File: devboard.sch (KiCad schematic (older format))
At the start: 100 parts, among them J1 Conn_01x04, J2 Conn_02x05_Odd_Even, J3 USB_B_Micro, J4 Conn_01x04, J5 Conn_02x10_Counter_Clockwise, J6 Conn_02x04_Counter_Clockwise, Q1 Q_NPN_BEC, Q2 Q_NPN_BEC, SW1 SW_SPST, U1 ATmega128L-8AU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

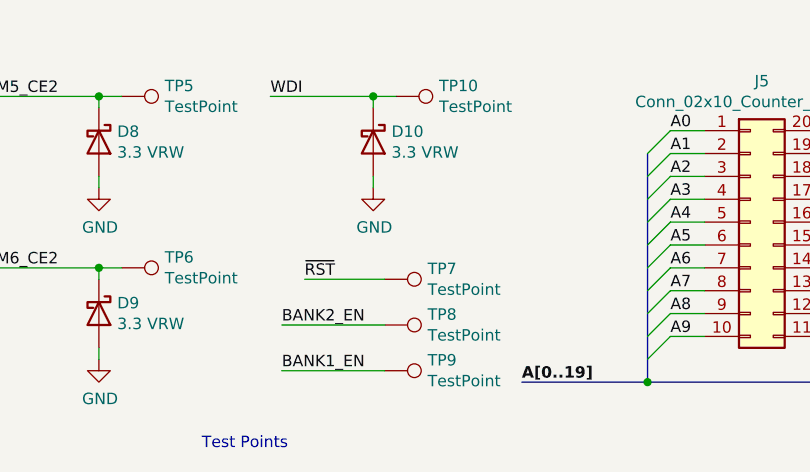
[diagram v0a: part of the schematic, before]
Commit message: Add 5V testpoint
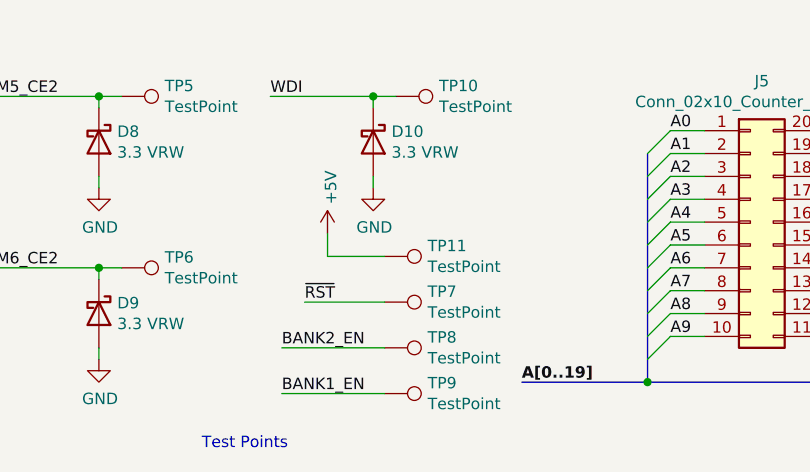
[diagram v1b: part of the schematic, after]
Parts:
- added TP11: TestPoint, Connector_PinHeader_2.54mm:PinHeader_1x01_P2.54mm_Vertical, symbol Connector:TestPoint
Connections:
- net +5V: now also TP11.1
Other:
- moved on the sheet: TP7, TP8, TP9
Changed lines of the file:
@@
 L Connector:TestPoint TP7
 U 1 1 6AC9D37E
-P 8100 10300
-F 0 "TP7" V 8054 10488 50  0000 L CNN
-F 1 "TestPoint" V 8145 10488 50  0000 L CNN
-F 2 "Connector_PinHeader_2.54mm:PinHeader_1x01_P2.54mm_Vertical" H 8300 10300 50  0001 C CNN
-F 3 "~" H 8300 10300 50  0001 C CNN
-	1    8100 10300
-	0    1    1    0
-$EndComp
-Wire Wire Line
-	7750 10300 8100 10300
-Text Label 7750 10300 0    50   ~ 0
+P 8100 10400
+F 0 "TP7" V 8054 10588 50  0000 L CNN
+F 1 "TestPoint" V 8145 10588 50  0000 L CNN
+F 2 "Connector_PinHeader_2.54mm:PinHeader_1x01_P2.54mm_Vertical" H 8300 10400 50  0001 C CNN
+F 3 "~" H 8300 10400 50  0001 C CNN
+	1    8100 10400
+	0    1    1    0
+$EndComp
+Wire Wire Line
+	7750 10400 8100 10400
+Text Label 7750 10400 0    50   ~ 0
 ~RST
 $Comp
 L Connector:TestPoint TP8
 U 1 1 6A948047
-P 8100 10500
-F 0 "TP8" V 8054 10688 50  0000 L CNN
-F 1 "TestPoint" V 8145 10688 50  0000 L CNN
-F 2 "Connector_PinHeader_2.54mm:PinHeader_1x01_P2.54mm_Vertical" H 8300 10500 50  0001 C CNN
-F 3 "~" H 8300 10500 50  0001 C CNN
-	1    8100 10500
+P 8100 10600
+F 0 "TP8" V 8054 10788 50  0000 L CNN
+F 1 "TestPoint" V 8145 10788 50  0000 L CNN
+F 2 "Connector_PinHeader_2.54mm:PinHeader_1x01_P2.54mm_Vertical" H 8300 10600 50  0001 C CNN
+F 3 "~" H 8300 10600 50  0001 C CNN
+	1    8100 10600
 	0    1    1    0
 $EndComp
@@
 L Connector:TestPoint TP9
 U 1 1 6A948041
-P 8100 10700
-F 0 "TP9" V 8054 10888 50  0000 L CNN
-F 1 "TestPoint" V 8145 10888 50  0000 L CNN
-F 2 "Connector_PinHeader_2.54mm:PinHeader_1x01_P2.54mm_Vertical" H 8300 10700 50  0001 C CNN
-F 3 "~" H 8300 10700 50  0001 C CNN
-	1    8100 10700
-	0    1    1    0
-$EndComp
-Text Label 7650 10500 0    50   ~ 0
+P 8100 10800
+F 0 "TP9" V 8054 10988 50  0000 L CNN
+F 1 "TestPoint" V 8145 10988 50  0000 L CNN
+F 2 "Connector_PinHeader_2.54mm:PinHeader_1x01_P2.54mm_Vertical" H 8300 10800 50  0001 C CNN
+F 3 "~" H 8300 10800 50  0001 C CNN
+	1    8100 10800
+	0    1    1    0
+$EndComp
+Text Label 7650 10600 0    50   ~ 0
 BANK2_EN
 Wire Wire Line
-	7650 10500 8100 10500
-Wire Wire Line
-	7650 10700 8100 10700
-Text Label 7650 10700 0    50   ~ 0
+	7650 10600 8100 10600
+Wire Wire Line
+	7650 10800 8100 10800
+Text Label 7650 10800 0    50   ~ 0
 BANK1_EN
 Connection ~ 9250 10750
@@
 Wire Wire Line
 	6550 1100 6600 1100
+$Comp
+L Connector:TestPoint TP11
+U 1 1 6F47491A
+P 8100 10200
+F 0 "TP11" V 8054 10388 50  0000 L CNN
+F 1 "TestPoint" V 8145 10388 50  0000 L CNN
+F 2 "Connector_PinHeader_2.54mm:PinHeader_1x01_P2.54mm_Vertical" H 8300 10200 50  0001 C CNN
+F 3 "~" H 8300 10200 50  0001 C CNN
+	1    8100 10200
+	0    1    1    0
+$EndComp
+$Comp
+L power:+5V #PWR0164
+U 1 1 6F4EB071
+P 7850 10100
+F 0 "#PWR0164" H 7850 9950 50  0001 C CNN
+F 1 "+5V" V 7865 10228 50  0000 L CNN
+F 2 "" H 7850 10100 50  0001 C CNN
+F 3 "" H 7850 10100 50  0001 C CNN
+	1    7850 10100
+	1    0    0    -1
+$EndComp
+Wire Wire Line
+	7850 10100 7850 10200
+Wire Wire Line
+	7850 10200 8100 10200
 Wire Bus Line
 	10700 10350 10700 10750

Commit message: Improve schematic labeling
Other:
- note added: "UART Bridge"
- note removed: "CRITICAL ELEMENTS:\nMCU\nReset circuit\nDebug circuit\nExternal tuning or clock oscillator?\nOBC connector testpads\nDedicated watchdog\nTest points"
- note removed: "Choose TWD, current selection is 3 seconds"
- note removed: "Current limiting on set shouldn't be necessary, check this"
- note removed: "Is a ferrite on the supply necessary in this application?"
- note removed: "LDO should be fine with ground\nplane. Shouldn't need to dissipate\nmore than 100 mW"
- note removed: "TODO:\nSerial headers"
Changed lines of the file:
@@
 Text Label 650  2200 0    50   ~ 0
 ~RST
-Text Notes 4650 2450 0    50   ~ 0
+Text Notes 4850 2450 0    50   ~ 0
 ATMega decoupling
 Text Label 1600 4700 0    50   ~ 0
@@
 Text Notes 550  2100 0    25   ~ 0
 Should the JTAG reset line be\nplaced before or after current\nlimiting?
-Text Notes 550  1250 0    50   ~ 0
-CRITICAL ELEMENTS:\nMCU\nReset circuit\nDebug circuit\nExternal tuning or clock oscillator?\nOBC connector testpads\nDedicated watchdog\nTest points
 NoConn ~ 2050 2800
 $Comp
@@
 	0    1    1    0
 $EndComp
-Text Notes 4900 1700 0    25   ~ 0
-Is a ferrite on the supply necessary in this application?
 Wire Wire Line
 	2650 1900 2650 1850
@@
 	1    0    0    -1
 $EndComp
-Text Notes 1550 9450 0    50   ~ 0
-Choose TWD, current selection is 3 seconds
-Text Notes 900  10550 0    25   ~ 0
-Current limiting on set shouldn't be necessary, check this
 $Comp
 L power:GND #PWR012
@@
 Wire Wire Line
 	1600 4700 2050 4700
-Text Notes 2150 700  0    50   ~ 0
-TODO:\nSerial headers
 $Comp
 L MCU_Microchip_ATmega:ATmega128L-8AU U1
@@
 	1    0    0    -1
 $EndComp
-Text Notes 12450 8550 0    25   ~ 0
-LDO should be fine with ground\nplane. Shouldn't need to dissipate\nmore than 100 mW
 Text Notes 12450 9550 0    50   ~ 0
 Supply Regulation
@@
 $EndComp
 NoConn ~ 14050 9250
-Text Notes 14050 9550 0    50   ~ 0
+Text Notes 13900 9550 0    50   ~ 0
 Debug Connector
 Wire Wire Line
@@
 Wire Wire Line
 	7850 10200 8100 10200
+Text Notes 2600 9100 0    50   ~ 0
+UART Bridge
 Wire Bus Line
 	10700 10350 10700 10750

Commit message: Fix attribution
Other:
- note added: "Daniel A. Stutman -2021"
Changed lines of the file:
@@
 Rev ""
 Comp ""
-Comment1 "Daniel A. Stutman"
+Comment1 ""
 Comment2 ""
 Comment3 ""
@@
 Wire Bus Line
 	8200 2000 8200 4050
+Text Notes 12000 10400 0    200  Italic 0
+Daniel A. Stutman -2021
 $EndSCHEMATC

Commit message: Fix UART lines
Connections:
- net UART_RX: now also U1.29 (PD4), U10.1 (TXD); no longer J1.2 (Pin_2), U1.28 (PD3), U10.5 (RXD)
- new net UART_TX: J1.2 (Pin_2), U1.28 (PD3), U10.5 (RXD)
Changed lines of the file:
@@
 Wire Wire Line
 	3750 5250 3750 7150
-Wire Wire Line
-	3900 5150 3900 5250
 $Comp
 L Device:C_Small C28
@@
 Wire Wire Line
 	4500 5500 4500 5250
-Wire Wire Line
-	4500 5250 3900 5250
-Connection ~ 3900 5250
-Wire Wire Line
-	3900 5250 3900 7250
 $Comp
 L power:GND #PWR0143
@@
 Text Notes 2600 9100 0    50   ~ 0
 UART Bridge
+Text Notes 12000 10400 0    200  Italic 0
+Daniel A. Stutman -2021
+Wire Wire Line
+	3900 5150 3900 7250
+Wire Wire Line
+	3750 5250 4500 5250
 Wire Bus Line
 	10700 10350 10700 10750
@@
 Wire Bus Line
 	8200 2000 8200 4050
-Text Notes 12000 10400 0    200  Italic 0
-Daniel A. Stutman -2021
+Connection ~ 3750 5250
 $EndSCHEMATC
